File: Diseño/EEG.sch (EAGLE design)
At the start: 28 parts, among them IC1 REF2033AIDDCT, IC2 MCP73831T-2ACI_OT, IC3 LP38692MP-3.3_NOPB, X1 MINI-USB_4P-85-32004-40X

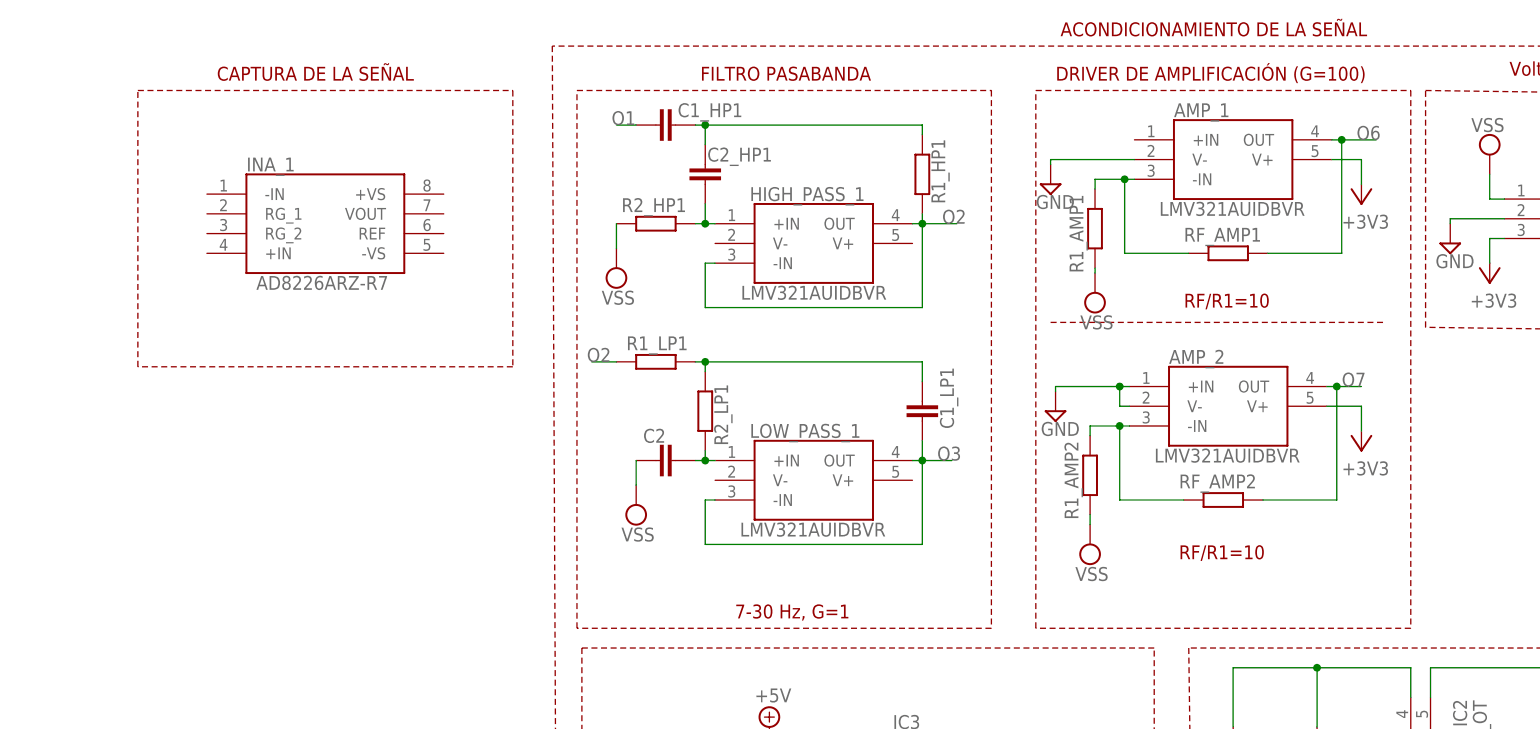
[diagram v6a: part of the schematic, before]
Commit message: Se estableció valores de resistores y capacitores para los filtros y amplificadores
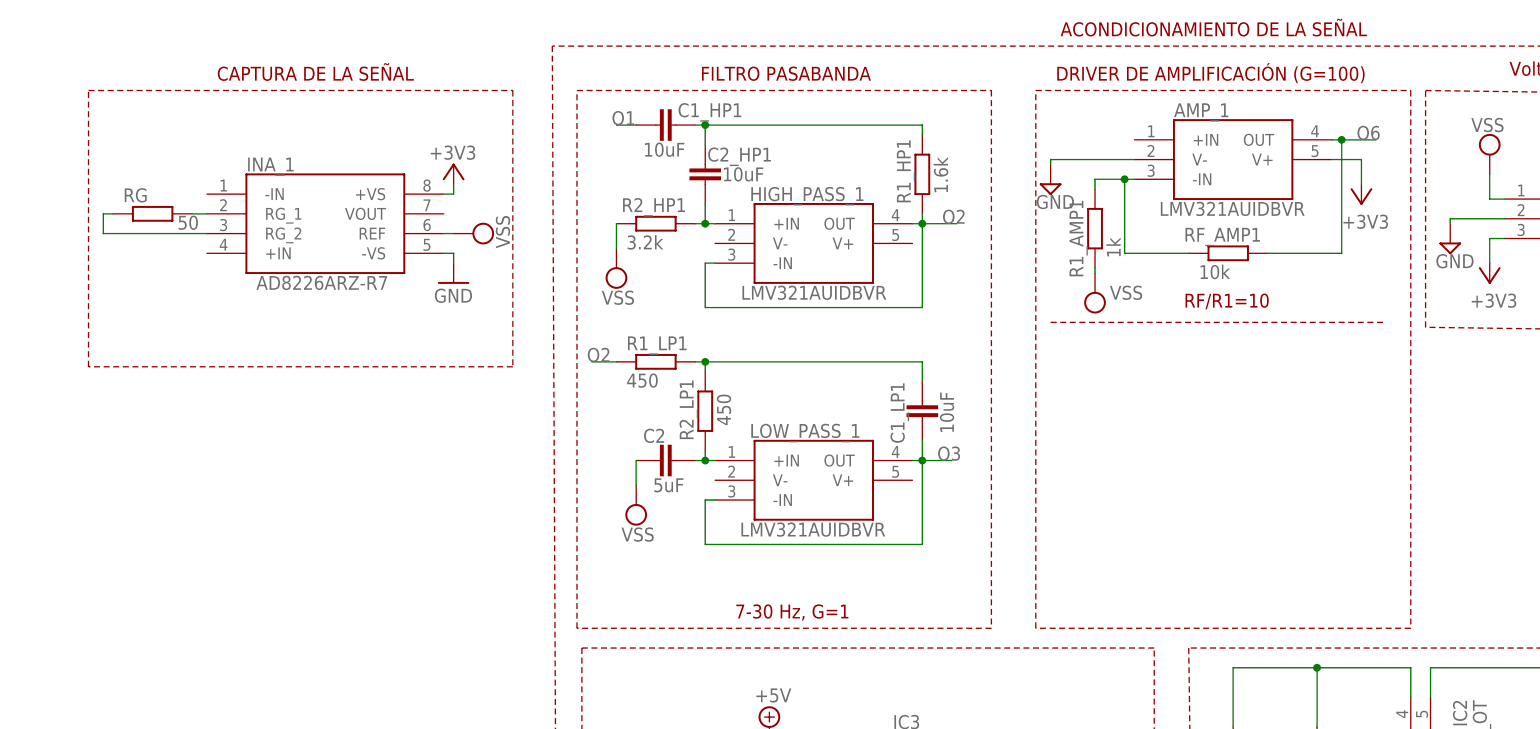
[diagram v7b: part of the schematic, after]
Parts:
- removed AMP_2: LMV321AUIDBVR, LMV321AUIDBVR:LMV321AUIDBVR
- removed R1_AMP2, RF_AMP2: (no value), rcl:R-EU_R0805
- added RG: 50, rcl:R-EU_M0805
- C1_HP1, C1_LP1, C2_HP1: value (none) -> 10uF
- C2: value (none) -> 5uF
- R1_AMP1: value (none) -> 1k
- R1_HP1: value (none) -> 1.6k
- R1_LP1, R2_LP1: value (none) -> 450
- R2_HP1: value (none) -> 3.2k
- RF_AMP1: value (none) -> 10k
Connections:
- removed net O7: AMP_2.OUT, RF_AMP2.2
- new net N$12: INA_1.RG_2, RG.1
- net +3V3: now also INA_1.+VS; no longer AMP_2.V+
- net GND: now also INA_1.-VS; no longer AMP_2.+IN, AMP_2.V-
- net N$9: now also INA_1.RG_1, RG.2; no longer AMP_2.-IN, R1_AMP2.2, RF_AMP2.1
- net VSS: now also INA_1.REF; no longer R1_AMP2.1

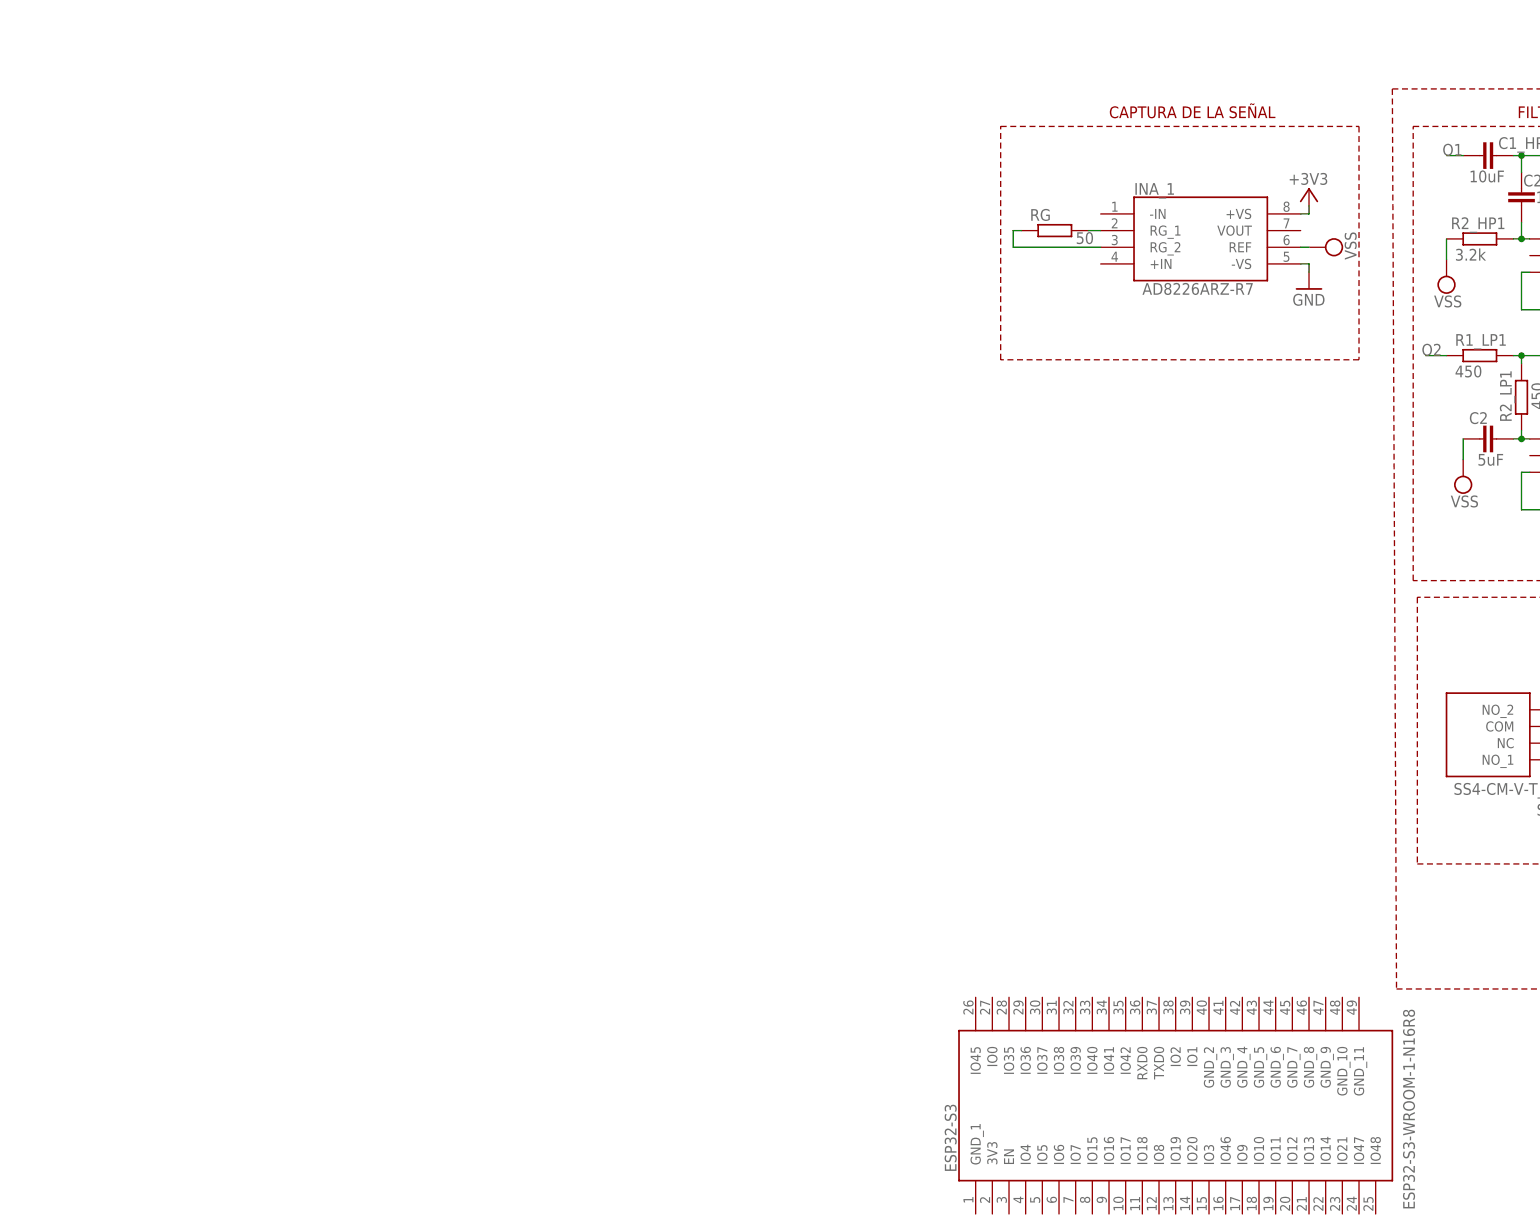
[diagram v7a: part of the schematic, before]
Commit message: Se subió circuito de la esp32 s3
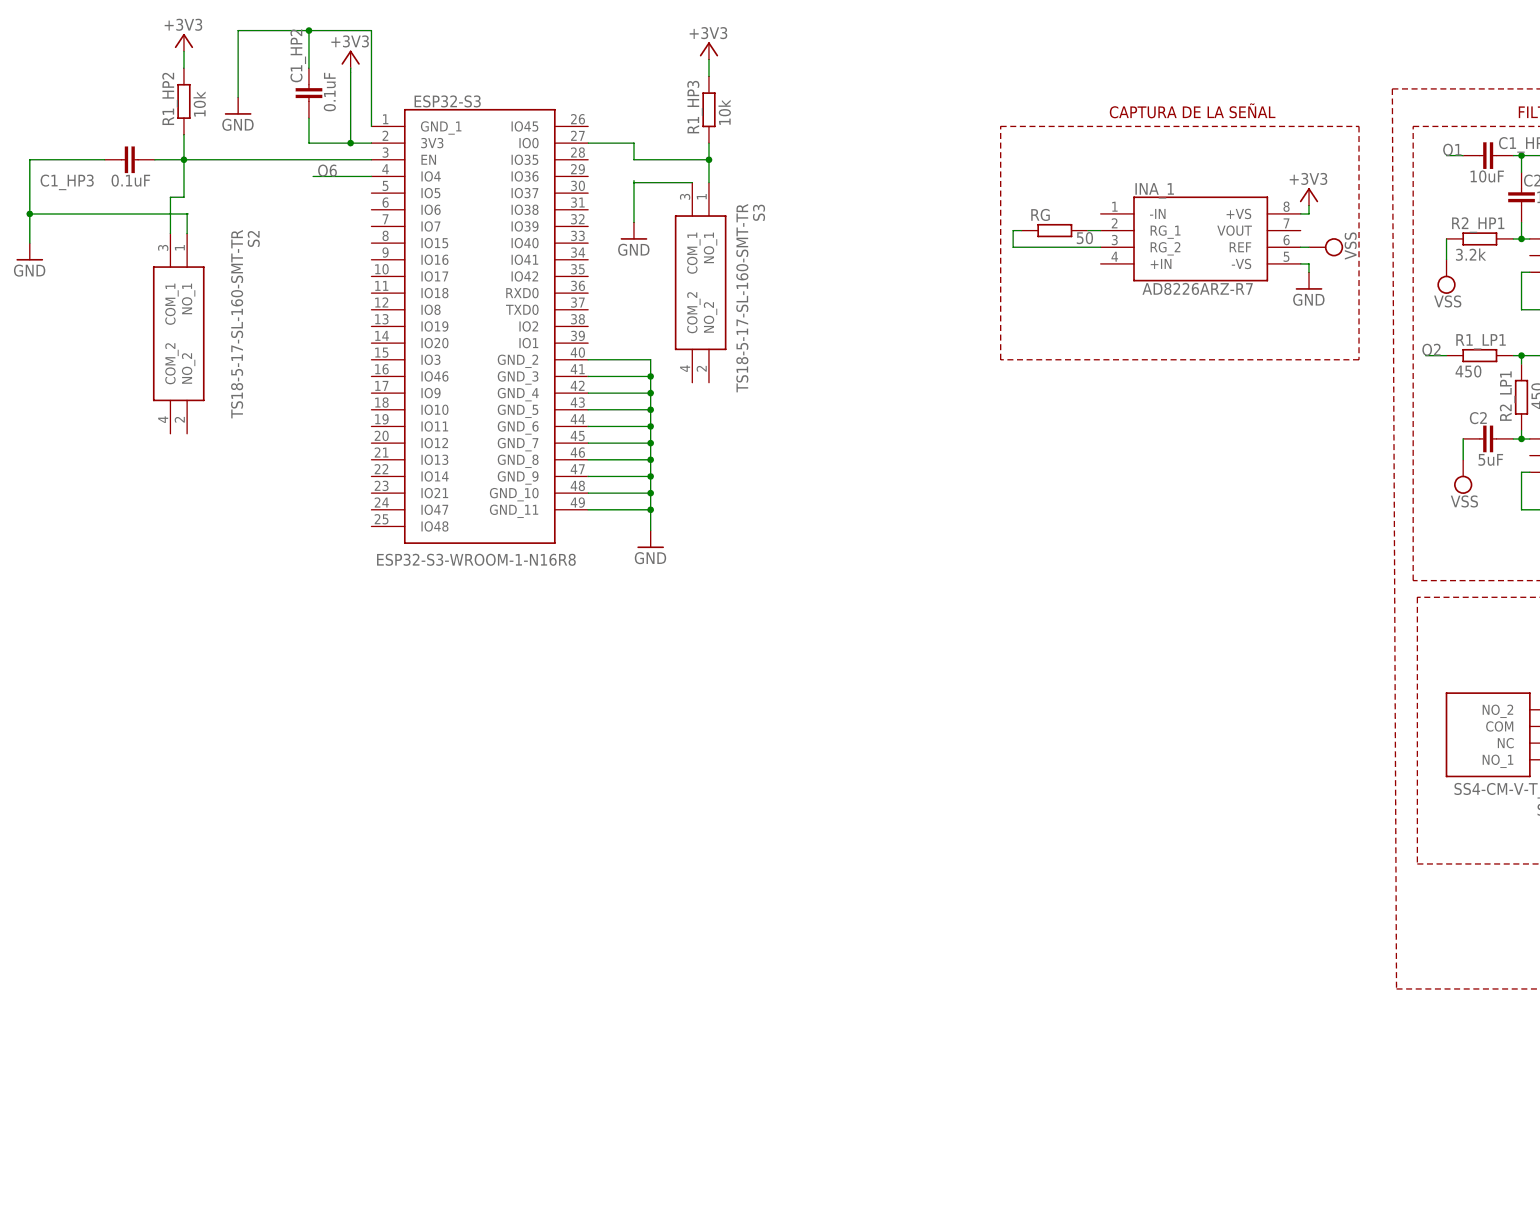
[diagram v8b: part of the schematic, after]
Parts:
- added C1_HP2, C1_HP3: 0.1uF, rcl:C-EUC0805
- added R1_HP2, R1_HP3: 10k, rcl:R-EU_R0805
- added S2, S3: TS18-5-17-SL-160-SMT-TR, TS18-5-17-SL-160-SMT-TR:TS18-5-17-SL-160-SMT-TR
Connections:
- new net N$13: ESP32-S3.IO0, R1_HP3.1, S3.NO_1
- new net N$15: C1_HP3.2, ESP32-S3.EN, R1_HP2.1, S2.COM_1
- net +3V3: now also C1_HP2.1, ESP32-S3.3V3, R1_HP2.2, R1_HP3.2
- net GND: now also C1_HP2.2, C1_HP3.1, ESP32-S3.GND_1, ESP32-S3.GND_10, ESP32-S3.GND_11, ESP32-S3.GND_2, ESP32-S3.GND_3, ESP32-S3.GND_4, ESP32-S3.GND_5, ESP32-S3.GND_6, ESP32-S3.GND_7, ESP32-S3.GND_8, ESP32-S3.GND_9, S2.NO_1, S3.COM_1
- net O6: now also ESP32-S3.IO4
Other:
- moved on the sheet: ESP32-S3
